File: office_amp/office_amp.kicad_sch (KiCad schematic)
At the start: 3 parts

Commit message: changes from tim and josef, prototype
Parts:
- added J4: Conn_01x08_Pin, symbol Connector:Conn_01x08_Pin
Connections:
- new net +12V: J4.3 (Pin_3)
- new net +5V: J4.4 (Pin_4)
- new net +5VA: J4.6 (Pin_6)
- new net -5V: J4.5 (Pin_5)
- new net -5VA: J4.7 (Pin_7)
- new net GNDREF: J4.1 (Pin_1)
- new net GND_Input: J4.8 (Pin_8)
- new net V+: J4.2 (Pin_2)

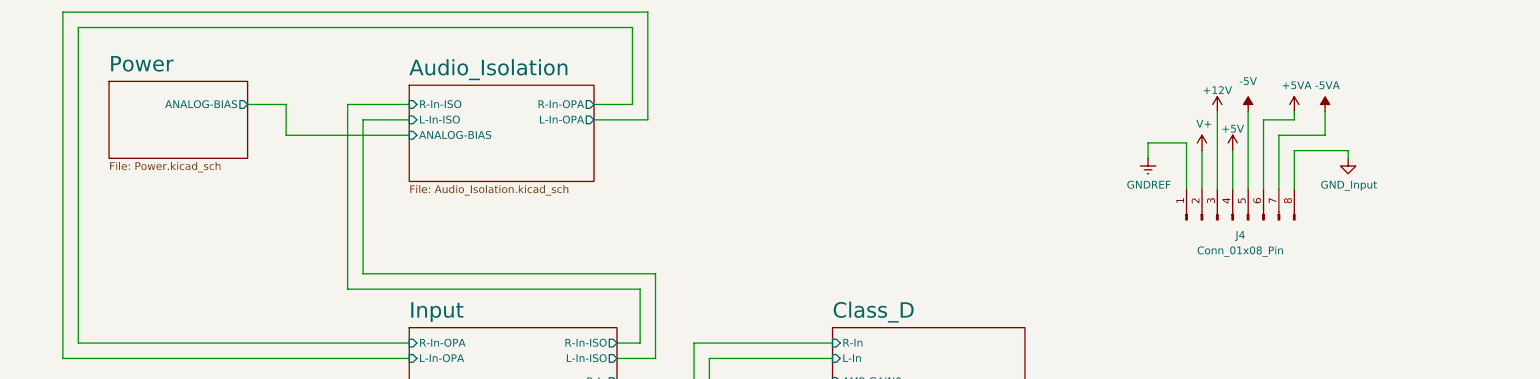
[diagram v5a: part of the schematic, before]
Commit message: splitted the prototype in 2 PCBs
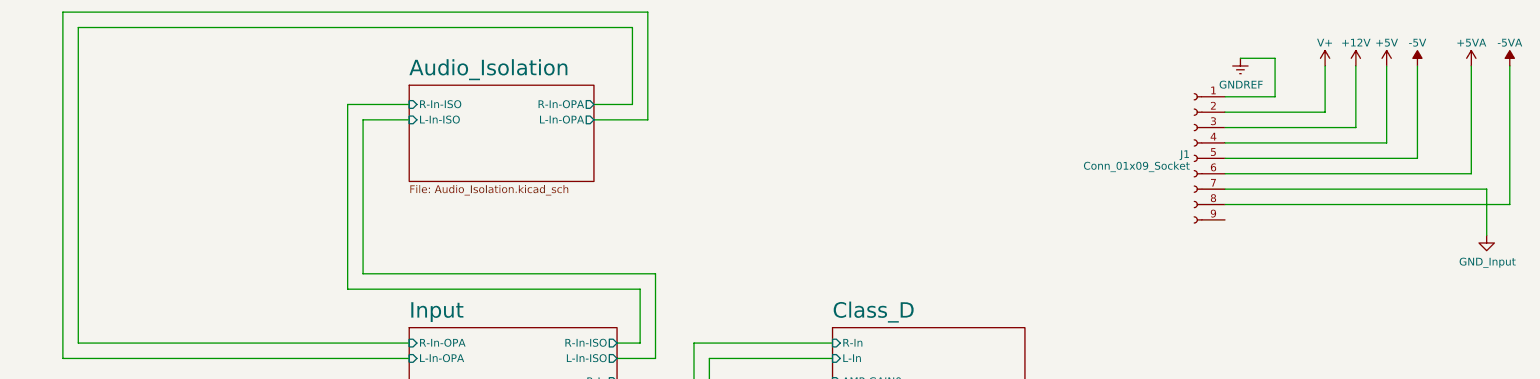
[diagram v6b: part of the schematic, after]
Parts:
- removed J4: Conn_01x08_Pin, symbol Connector:Conn_01x08_Pin
- added J1: Conn_01x09_Socket, Connector_Dsub:DSUB-9_Male_Horizontal_P2.77x2.84mm_EdgePinOffset4.94mm_Housed_MountingHolesOffset7.48mm, symbol Connector:Conn_01x09_Socket
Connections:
- net +12V: now also J1.3 (Pin_3)
- net +5V: now also J1.4 (Pin_4)
- net +5VA: now also J1.6 (Pin_6)
- net -5V: now also J1.5 (Pin_5)
- net -5VA: now also J1.8 (Pin_8)
- net GNDREF: now also J1.1 (Pin_1)
- net GND_Input: now also J1.7 (Pin_7)
- net V+: now also J1.2 (Pin_2)
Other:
- removed sheet Power
- sheet Audio_Isolation ports: added none; removed ANALOG-BIAS

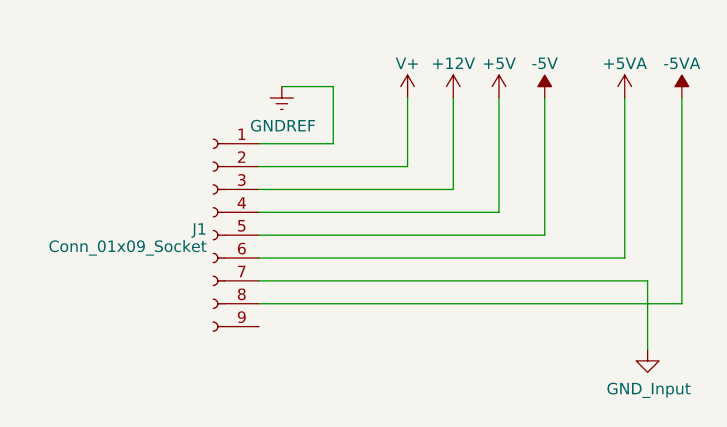
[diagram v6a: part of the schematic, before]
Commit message: first positioning office-amp
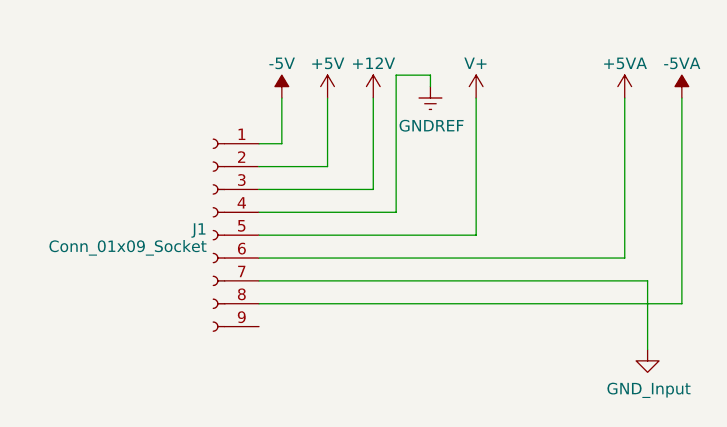
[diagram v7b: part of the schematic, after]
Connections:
- net +5V: now also J1.2 (Pin_2); no longer J1.4 (Pin_4)
- net -5V: now also J1.1 (Pin_1); no longer J1.5 (Pin_5)
- net GNDREF: now also J1.4 (Pin_4); no longer J1.1 (Pin_1)
- net V+: now also J1.5 (Pin_5); no longer J1.2 (Pin_2)
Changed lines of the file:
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@@
-    (stroke (width 0) (type default))
-  )
-  (wire (pts (xy 231.14 34.29) (xy 236.855 34.29))
     (stroke (width 0) (type default))
   )
@@
     (stroke (width 0) (type default))
   )
-  (wire (pts (xy 245.11 43.18) (xy 228.6 43.18))
-    (stroke (width 0) (type default))
-  )
   (wire (pts (xy 83.82 72.39) (xy 83.82 41.91))
     (stroke (width 0) (type default))
   )
-  (wire (pts (xy 255.27 48.26) (xy 228.6 48.26))
-    (stroke (width 0) (type default))
-  )
   (wire (pts (xy 83.82 41.91) (xy 93.98 41.91))
     (stroke (width 0) (type default))
   )
-  (wire (pts (xy 250.19 45.72) (xy 228.6 45.72))
+  (wire (pts (xy 241.3 45.72) (xy 228.6 45.72))
     (stroke (width 0) (type default))
   )
@@
     (stroke (width 0) (type default))
   )
-  (wire (pts (xy 260.35 35.56) (xy 260.35 50.8))
-    (stroke (width 0) (type default))
-  )
   (wire (pts (xy 133.35 26.67) (xy 36.83 26.67))
     (stroke (width 0) (type default))
@@
     (stroke (width 0) (type default))
   )
-  (wire (pts (xy 228.6 40.64) (xy 236.855 40.64))
+  (wire (pts (xy 243.84 48.26) (xy 243.84 33.02))
     (stroke (width 0) (type default))
   )
@@
     (stroke (width 0) (type default))
   )
+  (wire (pts (xy 228.6 48.26) (xy 243.84 48.26))
+    (stroke (width 0) (type default))
+  )
   (wire (pts (xy 148.59 90.17) (xy 163.83 90.17))
     (stroke (width 0) (type default))
   )
-  (wire (pts (xy 245.11 35.56) (xy 245.11 43.18))
-    (stroke (width 0) (type default))
-  )
-  (wire (pts (xy 255.27 35.56) (xy 255.27 48.26))
+  (wire (pts (xy 252.73 35.56) (xy 252.73 50.8))
+    (stroke (width 0) (type default))
+  )
+  (wire (pts (xy 231.14 35.56) (xy 231.14 40.64))
+    (stroke (width 0) (type default))
+  )
+  (wire (pts (xy 236.22 35.56) (xy 236.22 43.18))
     (stroke (width 0) (type default))
   )
@@
     (stroke (width 0) (type default))
   )
-  (wire (pts (xy 260.35 50.8) (xy 228.6 50.8))
+  (wire (pts (xy 228.6 50.8) (xy 252.73 50.8))
     (stroke (width 0) (type default))
   )
@@
     (stroke (width 0) (type default))
   )
-  (wire (pts (xy 236.855 40.64) (xy 236.855 34.29))
-    (stroke (width 0) (type default))
-  )
-  (wire (pts (xy 250.19 35.56) (xy 250.19 45.72))
+  (wire (pts (xy 241.3 35.56) (xy 241.3 45.72))
     (stroke (width 0) (type default))
   )
@@
     (stroke (width 0) (type default))
   )
+  (wire (pts (xy 243.84 33.02) (xy 247.65 33.02))
+    (stroke (width 0) (type default))
+  )
+  (wire (pts (xy 228.6 43.18) (xy 236.22 43.18))
+    (stroke (width 0) (type default))
+  )
+  (wire (pts (xy 228.6 40.64) (xy 231.14 40.64))
+    (stroke (width 0) (type default))
+  )
   (wire (pts (xy 143.51 90.17) (xy 143.51 83.82))
     (stroke (width 0) (type default))
   )
   (wire (pts (xy 128.27 106.68) (xy 158.75 106.68))
+    (stroke (width 0) (type default))
+  )
+  (wire (pts (xy 247.65 33.02) (xy 247.65 34.29))
     (stroke (width 0) (type default))
   )
@@
     )
   )
-  (symbol (lib_id "MyLib:V+") (at 245.11 35.56 0) (unit 1)
-    (in_bom yes) (on_board yes) (dnp no)
-    (property "Reference" "#PWR056" (at 245.11 39.37 0)
-      (effects (font (size 1.27 1.27)) hide)
-    )
-    (property "Value" "V+" (at 245.11 31.75 0)
-      (effects (font (size 1.27 1.27)))
-    )
-    (property "Footprint" "" (at 245.11 35.56 0)
-      (effects (font (size 1.27 1.27)) hide)
-    )
-    (property "Datasheet" "" (at 245.11 35.56 0)
+  (symbol (lib_id "MyLib:V+") (at 252.73 35.56 0) (unit 1)
+    (in_bom yes) (on_board yes) (dnp no)
+    (property "Reference" "#PWR071" (at 252.73 39.37 0)
+      (effects (font (size 1.27 1.27)) hide)
+    )
+    (property "Value" "V+" (at 252.73 31.75 0)
+      (effects (font (size 1.27 1.27)))
+    )
+    (property "Footprint" "" (at 252.73 35.56 0)
+      (effects (font (size 1.27 1.27)) hide)
+    )
+    (property "Datasheet" "" (at 252.73 35.56 0)
       (effects (font (size 1.27 1.27)) hide)
     )
@@
     )
   )
-  (symbol (lib_id "power:+5V") (at 255.27 35.56 0) (unit 1)
-    (in_bom yes) (on_board yes) (dnp no)
-    (property "Reference" "#PWR064" (at 255.27 39.37 0)
-      (effects (font (size 1.27 1.27)) hide)
-    )
-    (property "Value" "+5V" (at 255.27 31.75 0)
-      (effects (font (size 1.27 1.27)))
-    )
-    (property "Footprint" "" (at 255.27 35.56 0)
-      (effects (font (size 1.27 1.27)) hide)
-    )
-    (property "Datasheet" "" (at 255.27 35.56 0)
+  (symbol (lib_id "power:+5V") (at 236.22 35.56 0) (unit 1)
+    (in_bom yes) (on_board yes) (dnp no)
+    (property "Reference" "#PWR073" (at 236.22 39.37 0)
+      (effects (font (size 1.27 1.27)) hide)
+    )
+    (property "Value" "+5V" (at 236.22 31.75 0)
+      (effects (font (size 1.27 1.27)))
+    )
+    (property "Footprint" "" (at 236.22 35.56 0)
+      (effects (font (size 1.27 1.27)) hide)
+    )
+    (property "Datasheet" "" (at 236.22 35.56 0)
       (effects (font (size 1.27 1.27)) hide)
     )
@@
   (symbol (lib_id "power:+5VA") (at 269.24 35.56 0) (unit 1)
     (in_bom yes) (on_board yes) (dnp no)
-    (property "Reference" "#PWR067" (at 269.24 39.37 0)
+    (property "Reference" "#PWR075" (at 269.24 39.37 0)
       (effects (font (size 1.27 1.27)) hide)
     )
@@
     )
   )
-  (symbol (lib_id "power:+12V") (at 250.19 35.56 0) (unit 1)
-    (in_bom yes) (on_board yes) (dnp no)
-    (property "Reference" "#PWR062" (at 250.19 39.37 0)
-      (effects (font (size 1.27 1.27)) hide)
-    )
-    (property "Value" "+12V" (at 250.19 31.75 0)
-      (effects (font (size 1.27 1.27)))
-    )
-    (property "Footprint" "" (at 250.19 35.56 0)
-      (effects (font (size 1.27 1.27)) hide)
-    )
-    (property "Datasheet" "" (at 250.19 35.56 0)
+  (symbol (lib_id "power:+12V") (at 241.3 35.56 0) (unit 1)
+    (in_bom yes) (on_board yes) (dnp no)
+    (property "Reference" "#PWR072" (at 241.3 39.37 0)
+      (effects (font (size 1.27 1.27)) hide)
+    )
+    (property "Value" "+12V" (at 241.3 31.75 0)
+      (effects (font (size 1.27 1.27)))
+    )
+    (property "Footprint" "" (at 241.3 35.56 0)
+      (effects (font (size 1.27 1.27)) hide)
+    )
+    (property "Datasheet" "" (at 241.3 35.56 0)
       (effects (font (size 1.27 1.27)) hide)
     )
@@
     )
   )
-  (symbol (lib_id "power:GNDREF") (at 231.14 34.29 0) (unit 1)
-    (in_bom yes) (on_board yes) (dnp no)
-    (property "Reference" "#PWR066" (at 231.14 40.64 0)
-      (effects (font (size 1.27 1.27)) hide)
-    )
-    (property "Value" "GNDREF" (at 231.267 38.6842 0)
-      (effects (font (size 1.27 1.27)))
-    )
-    (property "Footprint" "" (at 231.14 34.29 0)
-      (effects (font (size 1.27 1.27)) hide)
-    )
-    (property "Datasheet" "" (at 231.14 34.29 0)
+  (symbol (lib_id "power:GNDREF") (at 247.65 34.29 0) (unit 1)
+    (in_bom yes) (on_board yes) (dnp no)
+    (property "Reference" "#PWR070" (at 247.65 40.64 0)
+      (effects (font (size 1.27 1.27)) hide)
+    )
+    (property "Value" "GNDREF" (at 247.777 38.6842 0)
+      (effects (font (size 1.27 1.27)))
+    )
+    (property "Footprint" "" (at 247.65 34.29 0)
+      (effects (font (size 1.27 1.27)) hide)
+    )
+    (property "Datasheet" "" (at 247.65 34.29 0)
       (effects (font (size 1.27 1.27)) hide)
     )
@@
   (symbol (lib_id "power:-5VA") (at 275.59 35.56 0) (unit 1)
     (in_bom yes) (on_board yes) (dnp no)
-    (property "Reference" "#PWR068" (at 275.59 33.02 0)
+    (property "Reference" "#PWR076" (at 275.59 33.02 0)
       (effects (font (size 1.27 1.27)) hide)
     )
@@
     )
   )
-  (symbol (lib_id "power:-5V") (at 260.35 35.56 0) (unit 1)
-    (in_bom yes) (on_board yes) (dnp no)
-    (property "Reference" "#PWR065" (at 260.35 33.02 0)
-      (effects (font (size 1.27 1.27)) hide)
-    )
-    (property "Value" "-5V" (at 260.35 31.75 0)
-      (effects (font (size 1.27 1.27)))
-    )
-    (property "Footprint" "" (at 260.35 35.56 0)
-      (effects (font (size 1.27 1.27)) hide)
-    )
-    (property "Datasheet" "" (at 260.35 35.56 0)
+  (symbol (lib_id "power:-5V") (at 231.14 35.56 0) (unit 1)
+    (in_bom yes) (on_board yes) (dnp no)
+    (property "Reference" "#PWR074" (at 231.14 33.02 0)
+      (effects (font (size 1.27 1.27)) hide)
+    )
+    (property "Value" "-5V" (at 231.14 31.75 0)
+      (effects (font (size 1.27 1.27)))
+    )
+    (property "Footprint" "" (at 231.14 35.56 0)
+      (effects (font (size 1.27 1.27)) hide)
+    )
+    (property "Datasheet" "" (at 231.14 35.56 0)
       (effects (font (size 1.27 1.27)) hide)
     )
@@
   (symbol (lib_id "OfficeAmp:GND_Input") (at 271.78 63.5 0) (unit 1)
     (in_bom yes) (on_board yes) (dnp no)
-    (property "Reference" "#PWR069" (at 271.78 69.85 0)
-      (effects (font (size 1.27 1.27)) hide)
-    )
+    (property "Reference" "#PWR077" (at 271.78 69.85 0)
+      (effects (font (size 1.27 1.27)) hide)
+    )

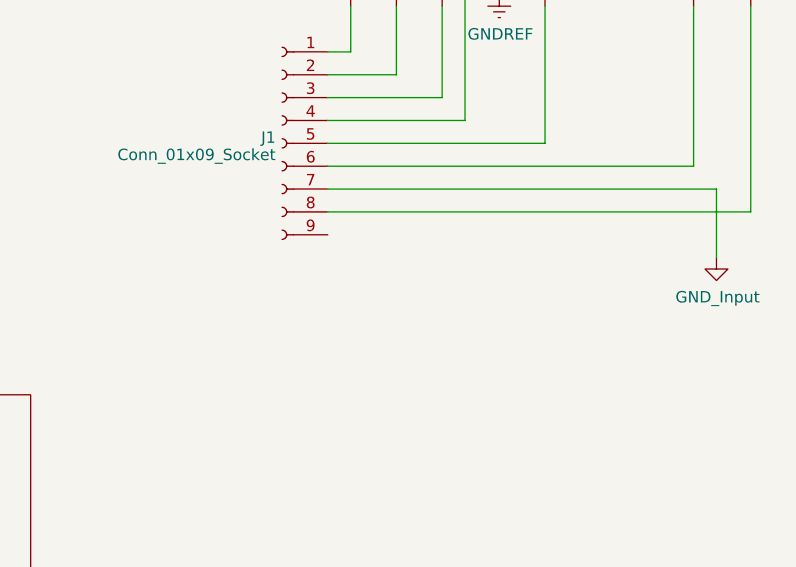
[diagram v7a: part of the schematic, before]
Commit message: Layout Amp done
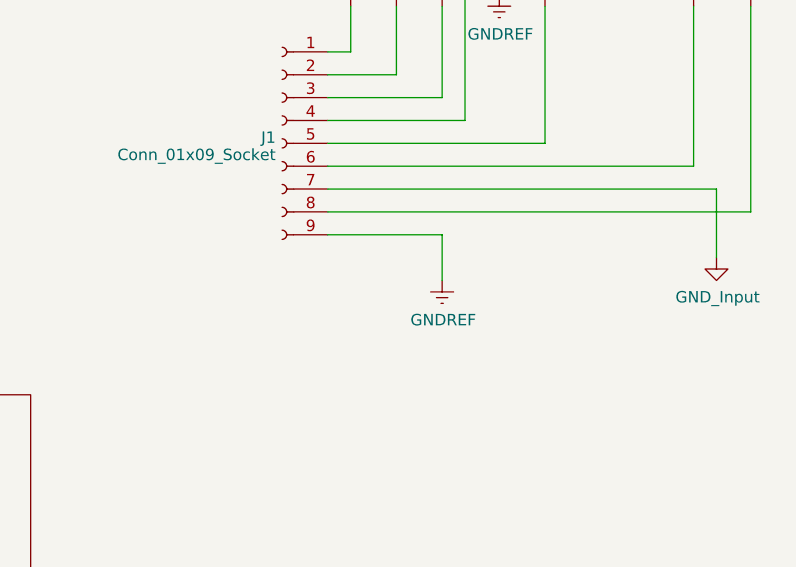
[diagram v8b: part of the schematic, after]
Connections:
- net GNDREF: now also J1.9 (Pin_9)
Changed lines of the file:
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@@
     (rev "1.3")
   )
+  (wire (pts (xy 241.3 66.04) (xy 241.3 60.96))
+    (stroke (width 0) (type default))
+  )
   (wire (pts (xy 153.67 101.6) (xy 153.67 95.25))
     (stroke (width 0) (type default))
@@
   )
   (wire (pts (xy 228.6 55.88) (xy 271.78 55.88))
+    (stroke (width 0) (type default))
+  )
+  (wire (pts (xy 241.3 60.96) (xy 228.6 60.96))
     (stroke (width 0) (type default))
   )
@@
         )
       )
+    )
+  )
+  (symbol (lib_id "power:GNDREF") (at 241.3 66.04 0) (unit 1)
+    (in_bom yes) (on_board yes) (dnp no)
+    (property "Reference" "#PWR01" (at 241.3 72.39 0)
+      (effects (font (size 1.27 1.27)) hide)
+    )
+    (property "Value" "GNDREF" (at 241.427 70.4342 0)
+      (effects (font (size 1.27 1.27)))
+    )
+    (property "Footprint" "" (at 241.3 66.04 0)
+      (effects (font (size 1.27 1.27)) hide)
+    )
+    (property "Datasheet" "" (at 241.3 66.04 0)
+      (effects (font (size 1.27 1.27)) hide)
+    )
+    (pin "1")
+    (instances
+      (project "office_amp"
+        (path "/2de1ffee-2174-41d2-8969-68b8d21e5a7d"
+          (reference "#PWR01") (unit 1)
+        )
+      )
